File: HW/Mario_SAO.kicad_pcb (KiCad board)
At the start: 2 copper layers, 57.5 x 67.5 mm, 13 parts, among them X1 Badgelife_sao_connector_v169b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

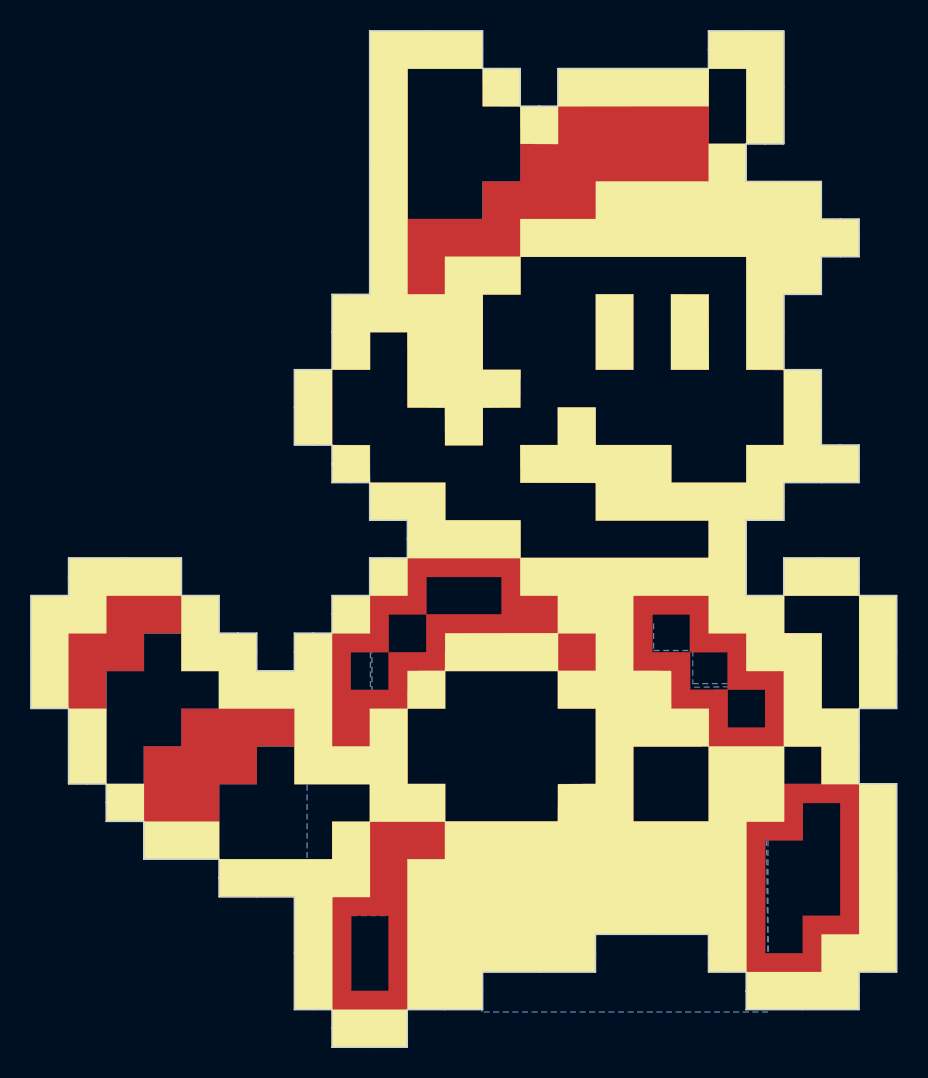
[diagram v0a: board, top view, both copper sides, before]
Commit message: fixed up art and moved an led.
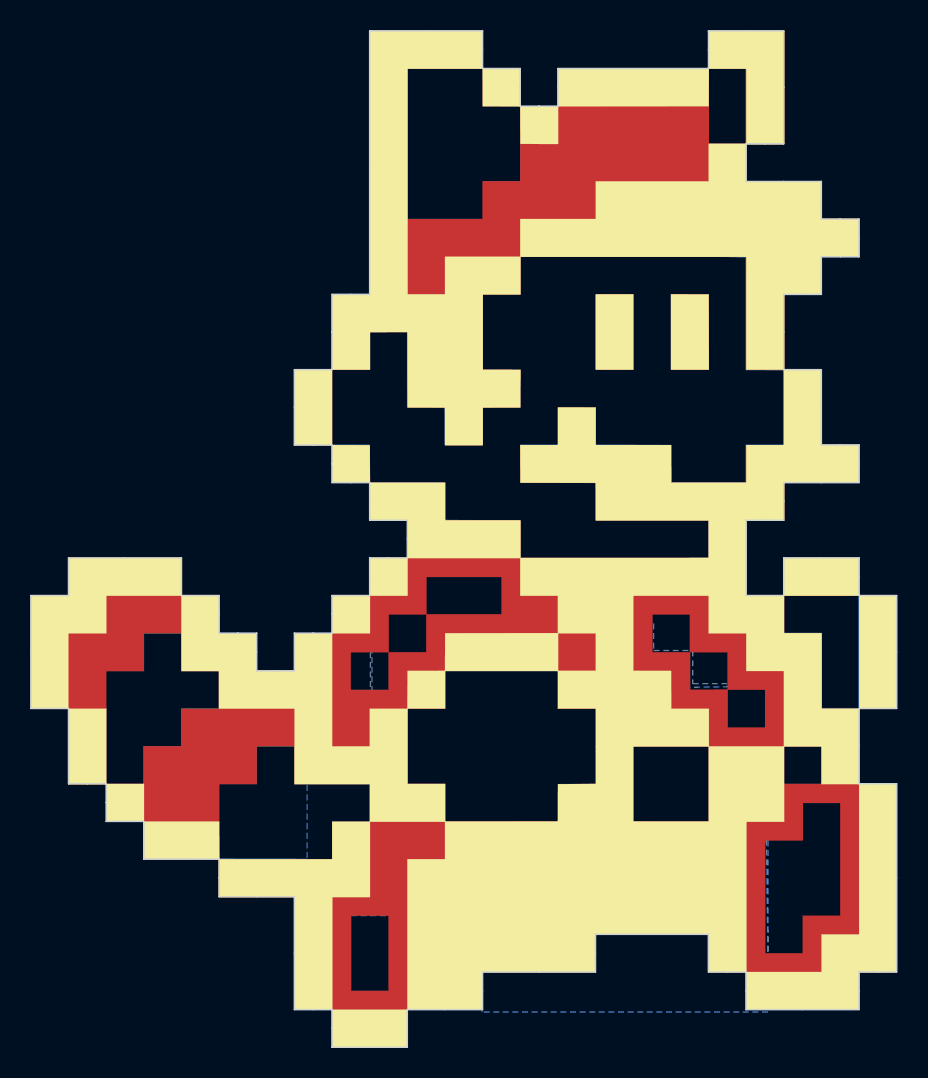
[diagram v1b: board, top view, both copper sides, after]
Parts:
- G***: value LOGO -> B.Silk
- G***: value LOGO -> B.Mask
- moved D4 3.72 mm to (112.5, 108.5), turned to 90 degrees
- moved R2 2.00 mm to (107.2, 107.0)
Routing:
- net Net-(D3-Pad2): track 18.6 -> 21.6 mm
- net VCC: track 26.6 -> 27.8 mm
